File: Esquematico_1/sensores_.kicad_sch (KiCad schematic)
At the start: 0 parts

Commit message: Carga de footprints
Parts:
- added C1: C, Capacitor_SMD:C_0805_2012Metric_Pad1.18x1.45mm_HandSolder, symbol Device:C
- added IC1: MAX-M10M-00B, MAX-M10M-00B:MAXM10M00B, symbol MAX-M10M-00B:MAX-M10M-00B
- added U1: Gyro, Tokmas ICM-42688-PC:LGA-14_L3.0-W2.5-P0.50-TL, symbol icm-42688-pc:ICM-42688-PC
- added U3: Mag, QMC588P:LGA-16_L3.0-W3.0-P0.50-BL_SQ, symbol qmc5883p:QMC5883P
- added U4: BMP388, BMP388:PQFN50P200X200X80-10N, symbol BMP388:BMP388
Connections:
- new net: U1.1 (SDO/SA0), U3.2 (VDD)
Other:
- note added: "Barometro"
- note added: "GPS"
- note added: "Gyroscopio"
- note added: "Magnometro"

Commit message: Kicad changes
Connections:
- net at U3.2 (VDD): no longer U1.1 (SDO/SA0)
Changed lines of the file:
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@@
-		)
-	)
-	(wire
-		(pts
-			(xy 78.74 20.32) (xy 78.74 34.29)
-		)
-		(stroke
-			(width 0)
-			(type default)
-		)
-	)
-	(wire
-		(pts
-			(xy 31.75 31.75) (xy 31.75 20.32)
-		)
-		(stroke
-			(width 0)
-			(type default)
-		)
-	)
-	(wire
-		(pts
-			(xy 78.74 34.29) (xy 87.63 34.29)
-		)
-		(stroke
-			(width 0)
-			(type default)
-		)
-	)
-	(wire
-		(pts
-			(xy 31.75 20.32) (xy 78.74 20.32)
-		)
-		(stroke
-			(width 0)
-			(type default)
 		)
 	)

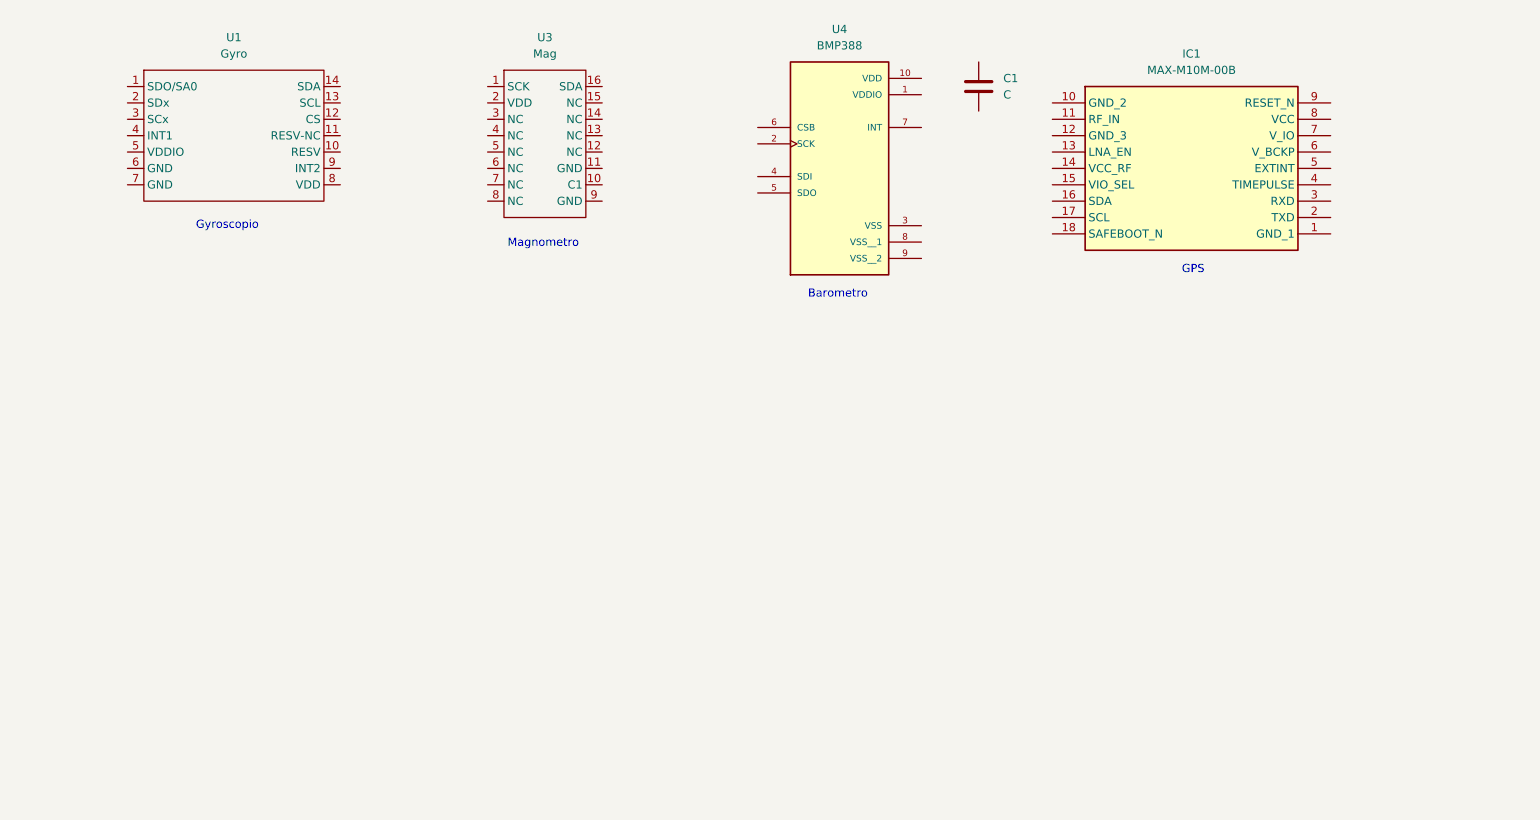
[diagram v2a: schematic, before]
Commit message: Conexion esqumatica del Magnetometro
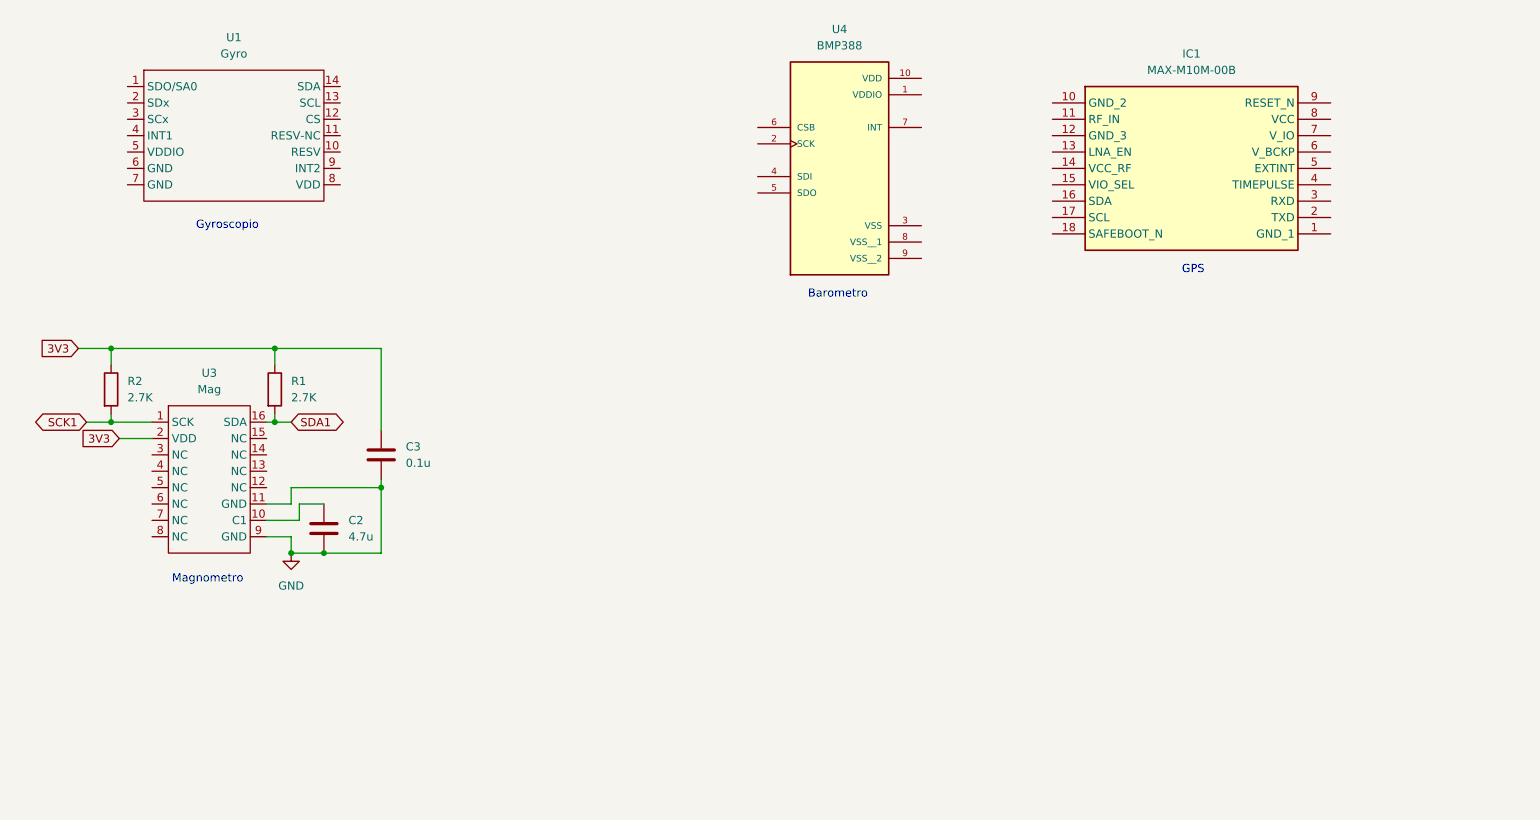
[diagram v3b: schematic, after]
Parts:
- removed C1: C, Capacitor_SMD:C_0805_2012Metric_Pad1.18x1.45mm_HandSolder, symbol Device:C
- added C2: 4.7u, symbol Device:C
- added C3: 0.1u, symbol Device:C
- added R1, R2: 2.7K, symbol Device:R
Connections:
- net SCK1: now reaches U3.1 (SCK)
- net SCK1: now also R2.2
- net at U3.10 (C1): now also C2.1
- net GND: now reaches U3.11 (GND)
- net GND: now also U3.9 (GND), C2.2, C3.2
- net SDA1: now reaches U3.16 (SDA)
- net SDA1: now also R1.2
- net 3V3: now reaches U3.2 (VDD)
- net 3V3: now also C3.1, R1.1, R2.1
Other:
- moved on the sheet: U3

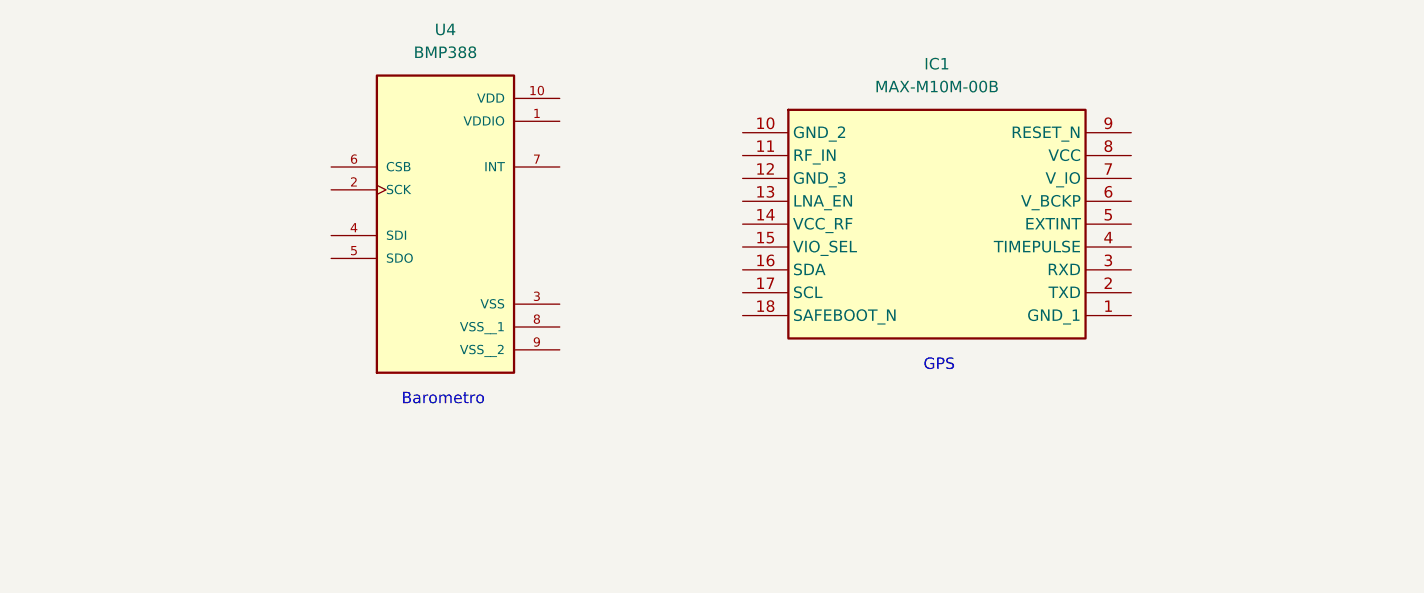
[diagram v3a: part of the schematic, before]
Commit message: Conexionado esquematico del Barometro
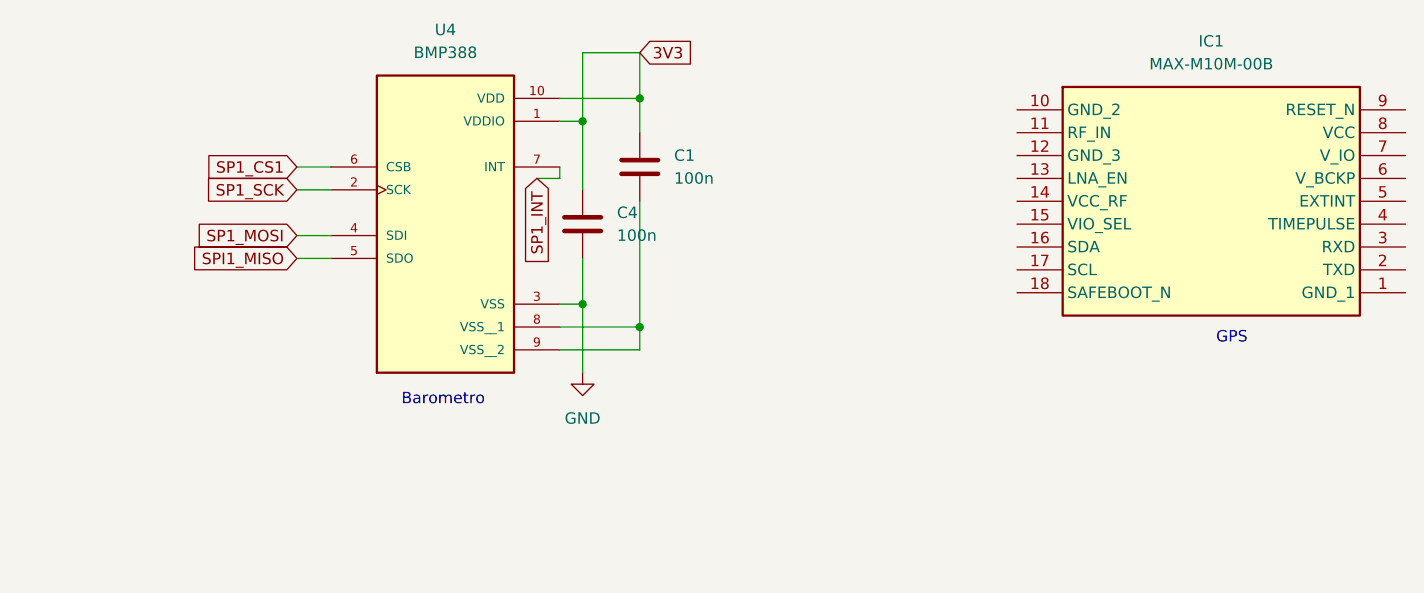
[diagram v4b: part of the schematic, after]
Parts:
- added C1, C4: 100n, symbol Device:C
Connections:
- net 3V3: now also U4.1 (VDDIO), U4.10 (VDD), C1.1, C4.1
- net GND: now also U4.3 (VSS), C4.2
- net SP1_SCK: now reaches U4.2 (SCK)
- net SP1_MOSI: now reaches U4.4 (SDI)
- net SPI1_MISO: now reaches U4.5 (SDO)
- net SP1_CS1: now reaches U4.6 (CSB)
- net SP1_INT: now reaches U4.7 (INT)
- net at U4.8 (VSS__1): now also U4.9 (VSS__2), C1.2
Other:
- moved on the sheet: IC1

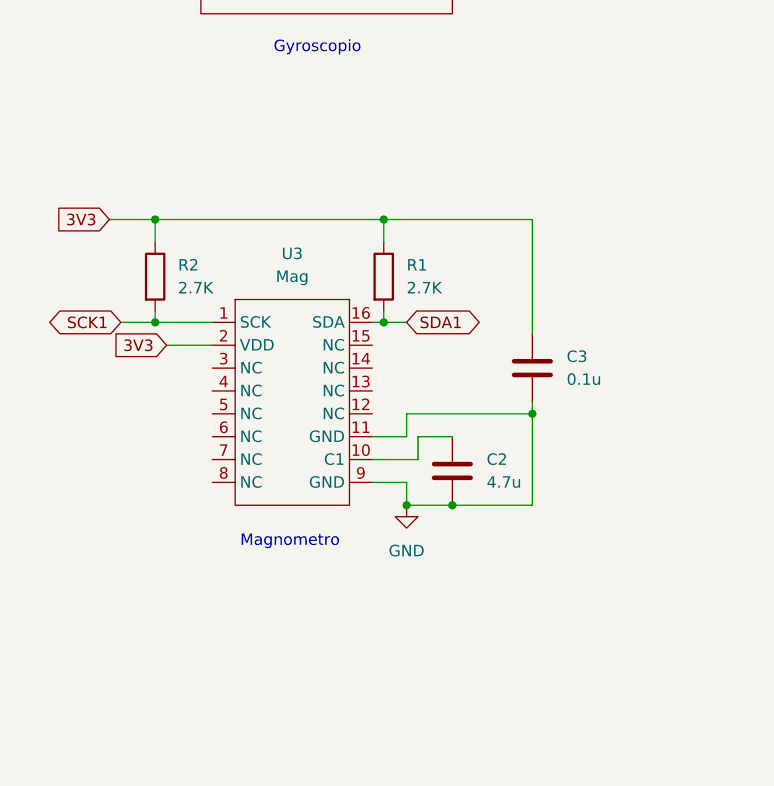
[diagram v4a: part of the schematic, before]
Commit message: Conexion esquematica Micro SD
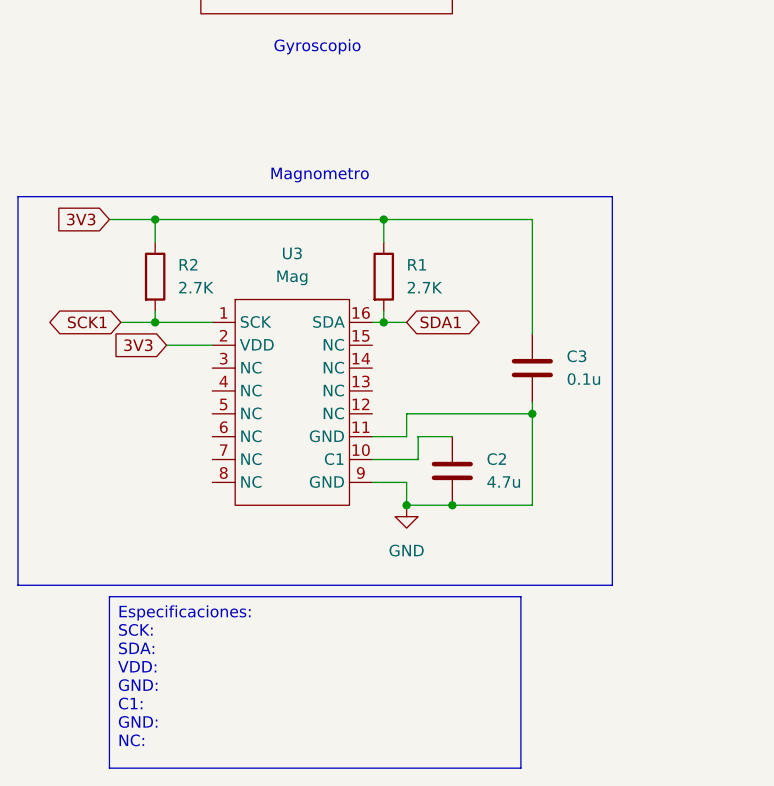
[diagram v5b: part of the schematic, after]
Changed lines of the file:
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@@
 	(generator_version "9.0")
 	(paper "A4")
+	(rectangle
+		(start 13.97 69.85)
+		(end 80.01 113.03)
+		(stroke
+			(width 0)
+			(type default)
+		)
+		(fill
+			(type none)
+		)
+	)
 	(text "Barometro\n"
 		(exclude_from_sim no)
@@
 	(text "Magnometro"
 		(exclude_from_sim no)
-		(at 44.196 108.204 0)
+		(at 47.498 67.564 0)
 		(effects
 			(font
@@
 		)
 	)
+	(text_box "Especificaciones:\nSCK:\nSDA:\nVDD:\nGND:\nC1:\nGND:\nNC:\n"
+		(exclude_from_sim no)
+		(at 24.13 114.3 0)
+		(size 45.72 19.05)
+		(margins 0.9525 0.9525 0.9525 0.9525)
+		(stroke
+			(width 0)
+			(type solid)
+		)
+		(fill
+			(type none)
+		)
+		(effects
+			(font
+				(size 1.27 1.27)
+			)
+			(justify left top)
+		)
+	)

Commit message: Descripcion de esquematicos
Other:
- moved on the sheet: C1, C4, U4
